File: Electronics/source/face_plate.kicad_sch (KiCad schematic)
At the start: 1 part, among them SW1 SW_Push

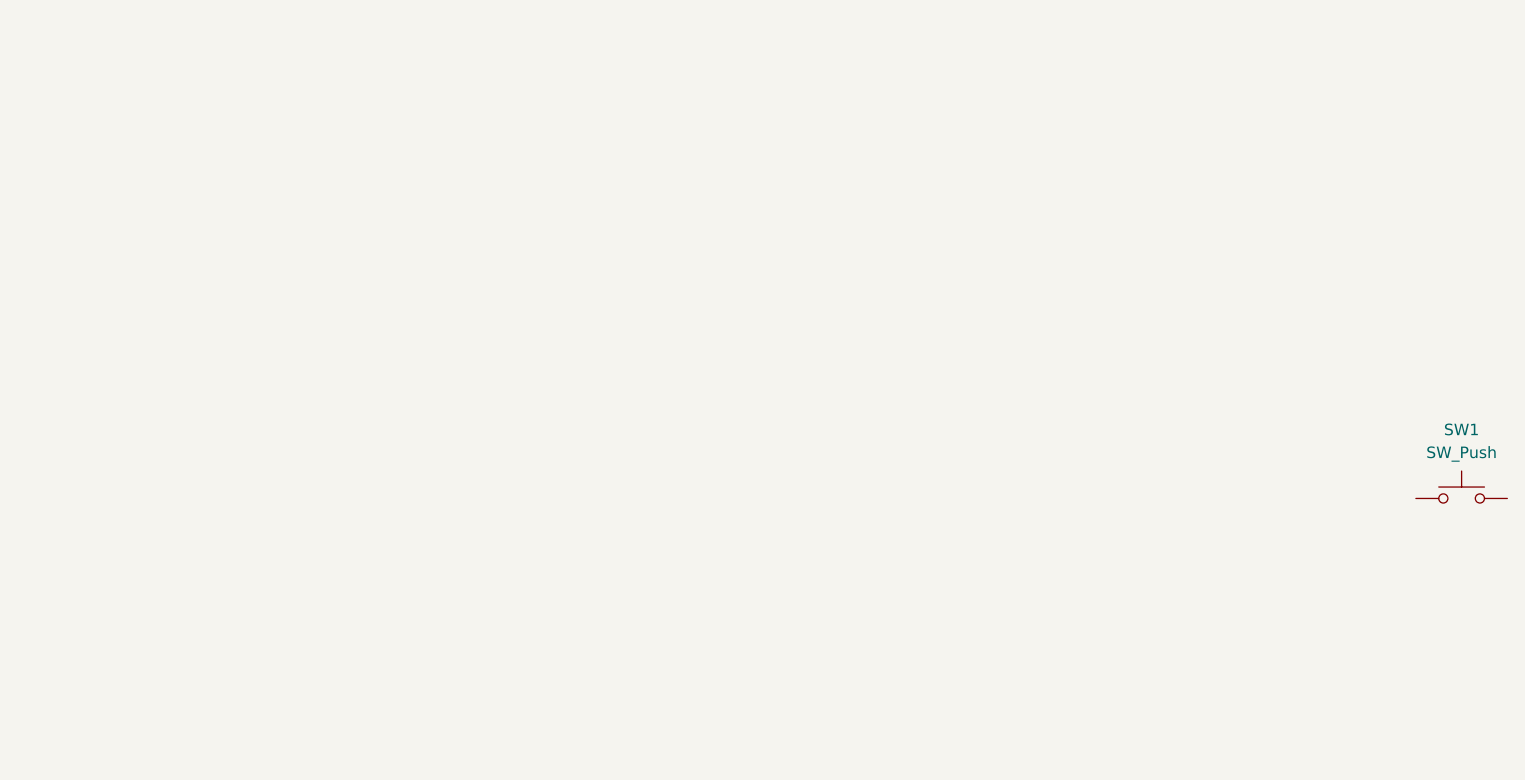
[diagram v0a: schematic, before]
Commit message: started layout and finished board shapes
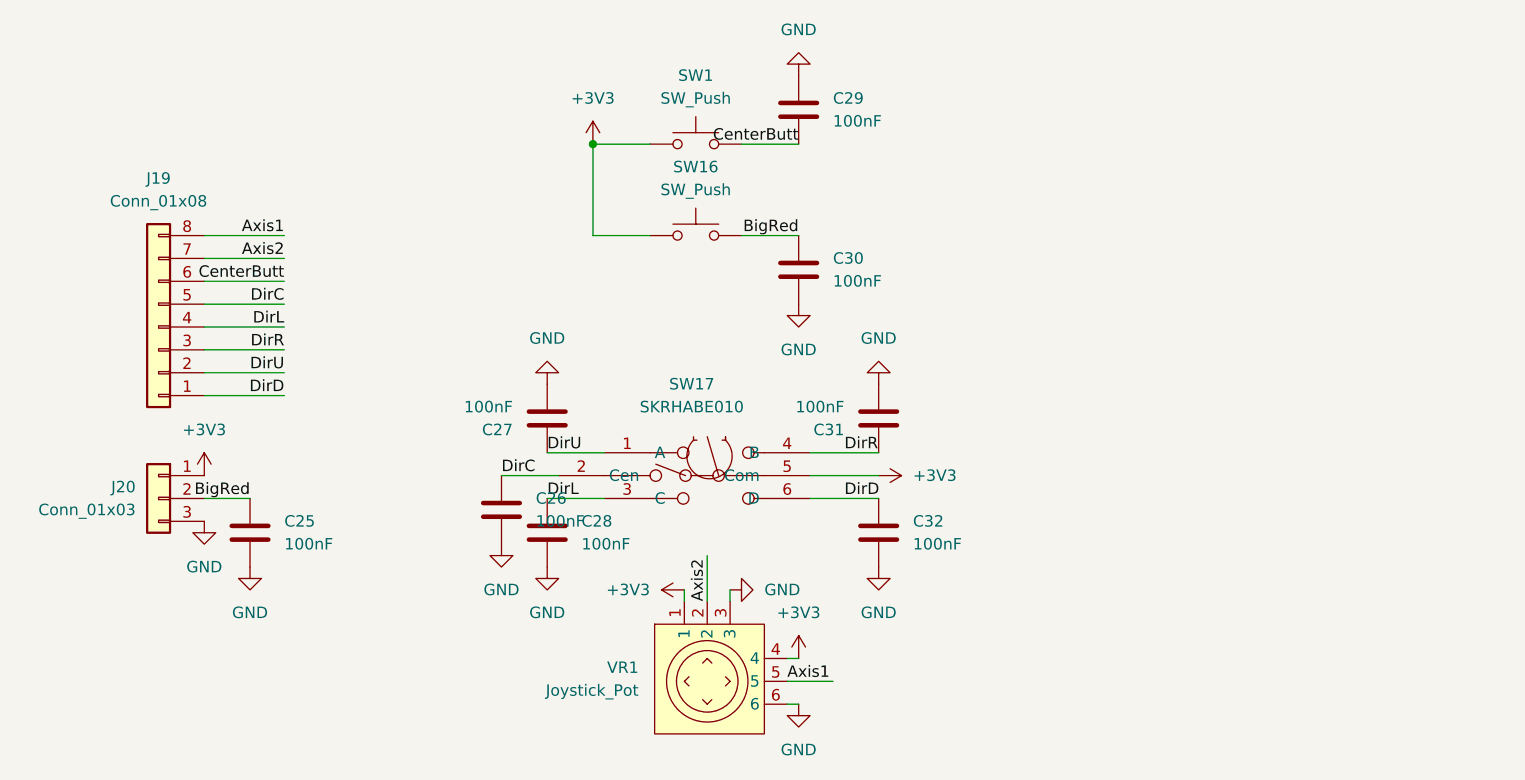
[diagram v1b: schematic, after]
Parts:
- added C25, C26, C27, C28, C29, C30, C31, C32: 100nF, Capacitor_SMD:C_0805_2012Metric, symbol Device:C
- added J19: Conn_01x08, Connector_JST:JST_PH_S8B-PH-K_1x08_P2.00mm_Horizontal, symbol Connector_Generic:Conn_01x08
- added J20: Conn_01x03, Connector_JST:JST_PH_B3B-PH-K_1x03_P2.00mm_Vertical, symbol Connector_Generic:Conn_01x03
- added SW16: SW_Push, Personal:PS1024AL, symbol Switch:SW_Push
- added SW17: SKRHABE010, Personal:SKRHABE010, symbol Personal:SKRHABE010
- added VR1: Joystick_Pot, Personal:RKJXV1220, symbol Personal:Joystick_Pot
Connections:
- net +3V3: now reaches SW1.1
- net +3V3: now also J20.1 (Pin_1), SW16.1, SW17.5 (Com), VR1.1, VR1.4
- net CenterButt: now reaches SW1.2
- net CenterButt: now also C29.1, J19.6 (Pin_6)
- new net Axis1: J19.8 (Pin_8), VR1.5
- new net Axis2: J19.7 (Pin_7), VR1.2
- new net BigRed: C25.1, C30.1, J20.2 (Pin_2), SW16.2
- new net DirC: C26.1, J19.5 (Pin_5), SW17.2 (Cen)
- new net DirD: C32.1, J19.1 (Pin_1), SW17.6 (D)
- new net DirL: C28.1, J19.4 (Pin_4), SW17.3 (C)
- new net DirR: C31.1, J19.3 (Pin_3), SW17.4 (B)
- new net DirU: C27.1, J19.2 (Pin_2), SW17.1 (A)
- new net GND: C25.2, C26.2, C27.2, C28.2, C29.2, C30.2, C31.2, C32.2, J20.3 (Pin_3), VR1.3, VR1.6
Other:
- moved on the sheet: SW1
